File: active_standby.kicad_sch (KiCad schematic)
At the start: 14 parts, among them Q2 BSS138, U24 SN3257QDYYRQ1, U30 SN3257QDYYRQ1

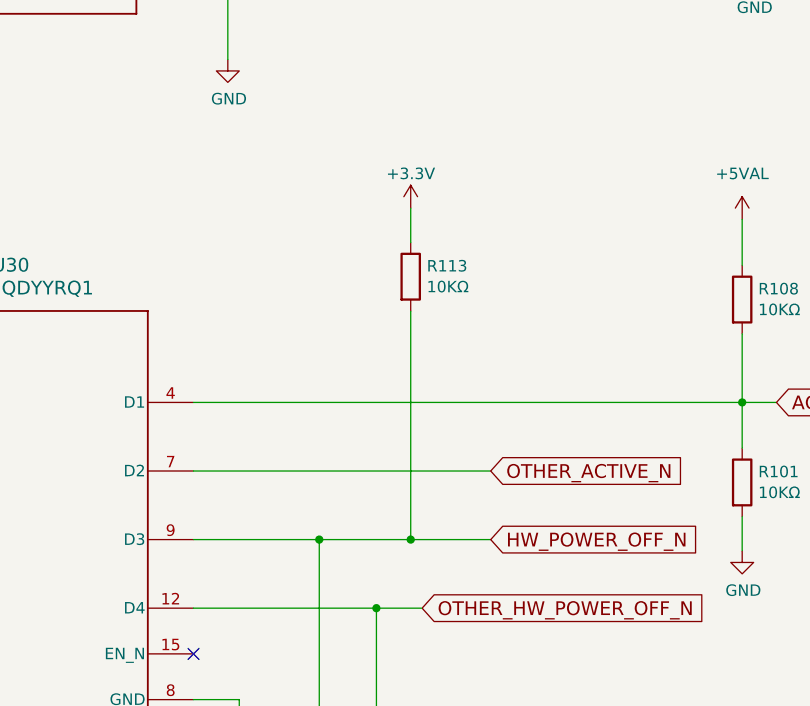
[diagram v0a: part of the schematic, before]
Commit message: Remove extra pullup from HW_POWER_OFF_N
One was going to 3.3V and then a +5V to ground dividier.  The
3.3V one was not going to work, as that wasn't powered up in
time.

Signed-off-by: Corey Minyard <corey@minyard.net>
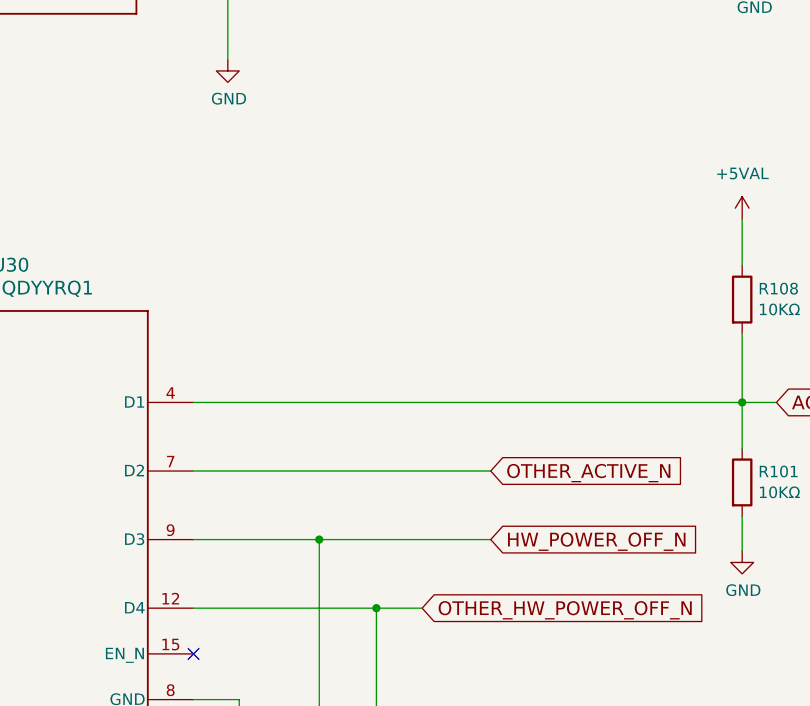
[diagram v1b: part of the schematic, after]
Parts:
- removed R113: 10KΩ, Resistor_SMD:R_0402_1005Metric_Pad0.72x0.64mm_HandSolder, symbol Device:R
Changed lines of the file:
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@@
-	)
-	(junction
-		(at 134.62 140.97)
-		(diameter 0)
-		(color 0 0 0 0)
 	)
 	(junction
@@
 	(wire
 		(pts
-			(xy 124.46 140.97) (xy 134.62 140.97)
+			(xy 124.46 140.97) (xy 143.51 140.97)
 		)
 		(stroke
@@
 	(wire
 		(pts
-			(xy 134.62 140.97) (xy 143.51 140.97)
-		)
-		(stroke
-			(width 0)
-			(type default)
-		)
-	)
-	(wire
-		(pts
 			(xy 63.5 49.53) (xy 63.5 54.61)
 		)
@@
 		(pts
 			(xy 110.49 133.35) (xy 143.51 133.35)
-		)
-		(stroke
-			(width 0)
-			(type default)
-		)
-	)
-	(wire
-		(pts
-			(xy 134.62 104.14) (xy 134.62 107.95)
-		)
-		(stroke
-			(width 0)
-			(type default)
-		)
-	)
-	(wire
-		(pts
-			(xy 134.62 115.57) (xy 134.62 140.97)
 		)
 		(stroke
@@
 	)
 	(symbol
-		(lib_id "power:+3.3V")
-		(at 134.62 104.14 0)
-		(unit 1)
-		(exclude_from_sim no)
-		(in_bom yes)
-		(on_board yes)
-		(dnp no)
-		(fields_autoplaced yes)
-		(property "Reference" "#PWR0268"
-			(at 134.62 107.95 0)
-			(effects
-				(font
-					(size 1.27 1.27)
-				)
-				(hide yes)
-			)
-		)
-		(property "Value" "+3.3V"
-			(at 134.62 100.33 0)
-			(effects
-				(font
-					(size 1.27 1.27)
-				)
-			)
-		)
-		(property "Footprint" ""
-			(at 134.62 104.14 0)
-			(effects
-				(font
-					(size 1.27 1.27)
-				)
-				(hide yes)
-			)
-		)
-		(property "Datasheet" ""
-			(at 134.62 104.14 0)
-			(effects
-				(font
-					(size 1.27 1.27)
-				)
-				(hide yes)
-			)
-		)
-		(property "Description" ""
-			(at 134.62 104.14 0)
-			(effects
-				(font
-					(size 1.27 1.27)
-				)
-			)
-		)
-		(pin "1"
-		)
-		(instances
-			(project "PacSat_AFSK"
-				(path "/cc9f42d2-6985-41ac-acab-5ab7b01c5b38/4fa888af-703c-49ed-93bb-d56d2f02c470"
-					(reference "#PWR0268")
-					(unit 1)
-				)
-			)
-		)
-	)
-	(symbol
 		(lib_id "Transistor_FET:BSS138")
 		(at 133.35 168.91 0)
@@
 					(unit 1)
 				)
-			)
-		)
-	)
-	(symbol
-		(lib_id "Device:R")
-		(at 134.62 111.76 0)
-		(unit 1)
-		(exclude_from_sim no)
-		(in_bom yes)
-		(on_board yes)
-		(dnp no)
-		(property "Reference" "R113"
-			(at 136.398 110.5916 0)
-			(effects
-				(font
-					(size 1.27 1.27)
-				)
-				(justify left)
-			)
-		)
-		(property "Value" "10KΩ"
-			(at 136.398 112.903 0)
-			(effects
-				(font
-					(size 1.27 1.27)
-				)
-				(justify left)
-			)
-		)
-		(property "Footprint" "Resistor_SMD:R_0402_1005Metric_Pad0.72x0.64mm_HandSolder"
-			(at 132.842 111.76 90)
-			(effects
-				(font
-					(size 1.27 1.27)
-				)
-				(hide yes)
-			)
-		)
-		(property "Datasheet" "~"
-			(at 134.62 111.76 0)
-			(effects
-				(font
-					(size 1.27 1.27)
-				)
-				(hide yes)
-			)
-		)
-		(property "Description" ""
-			(at 134.62 111.76 0)
-			(effects
-				(font
-					(size 1.27 1.27)
-				)
-			)
-		)
-		(pin "1"
-		)
-		(pin "2"
-		)
-		(instances
-			(project "PacSat_AFSK"
-				(path "/cc9f42d2-6985-41ac-acab-5ab7b01c5b38/4fa888af-703c-49ed-93bb-d56d2f02c470"
-					(reference "R113")
-					(unit 1)
-				)
